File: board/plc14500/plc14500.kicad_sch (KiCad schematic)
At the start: 8 parts

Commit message: REV.D Schema updates
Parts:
- removed C? (x4): 100nF, Capacitor_THT:C_Rect_L7.2mm_W2.5mm_P5.00mm_FKS2_FKP2_MKS2_MKP2, symbol Device:C
- removed U? (x3): 74HC14, Package_DIP:DIP-14_W7.62mm_LongPads, symbol 74xx:74HC14
- removed U?: 4011, Package_DIP:DIP-14_W7.62mm_LongPads, symbol 4xxx:4011
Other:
- sheet Input/Output renamed Input-Output
- added sheet Programming Interface (programming_if.kicad_sch)
- sheet CPU ports: added A0, A1, A2, A3, A4, A5, A6, A7, D, D0, D1, D2, D3, D4, D5, D6, D7, PRG, RES, RR, W, WEN; removed none
- sheet Input-Output ports: added !RES, A0, A1, A2, A3, A4, A5, A6, A7, D, D0, D1, D2, D3, D4, D5, D6, D7, IN-INH, OUT-WD, OUT0, OUT1, OUT2, OUT3, OUT4, OUT5, OUT6, OUT7, PRG, RES, TMR0-TRG, WEN; removed none
- sheet SPRAM ports: added D, D4, D5, D6, D7, IN-INH, OUT-WD, RES, RR, W; removed none

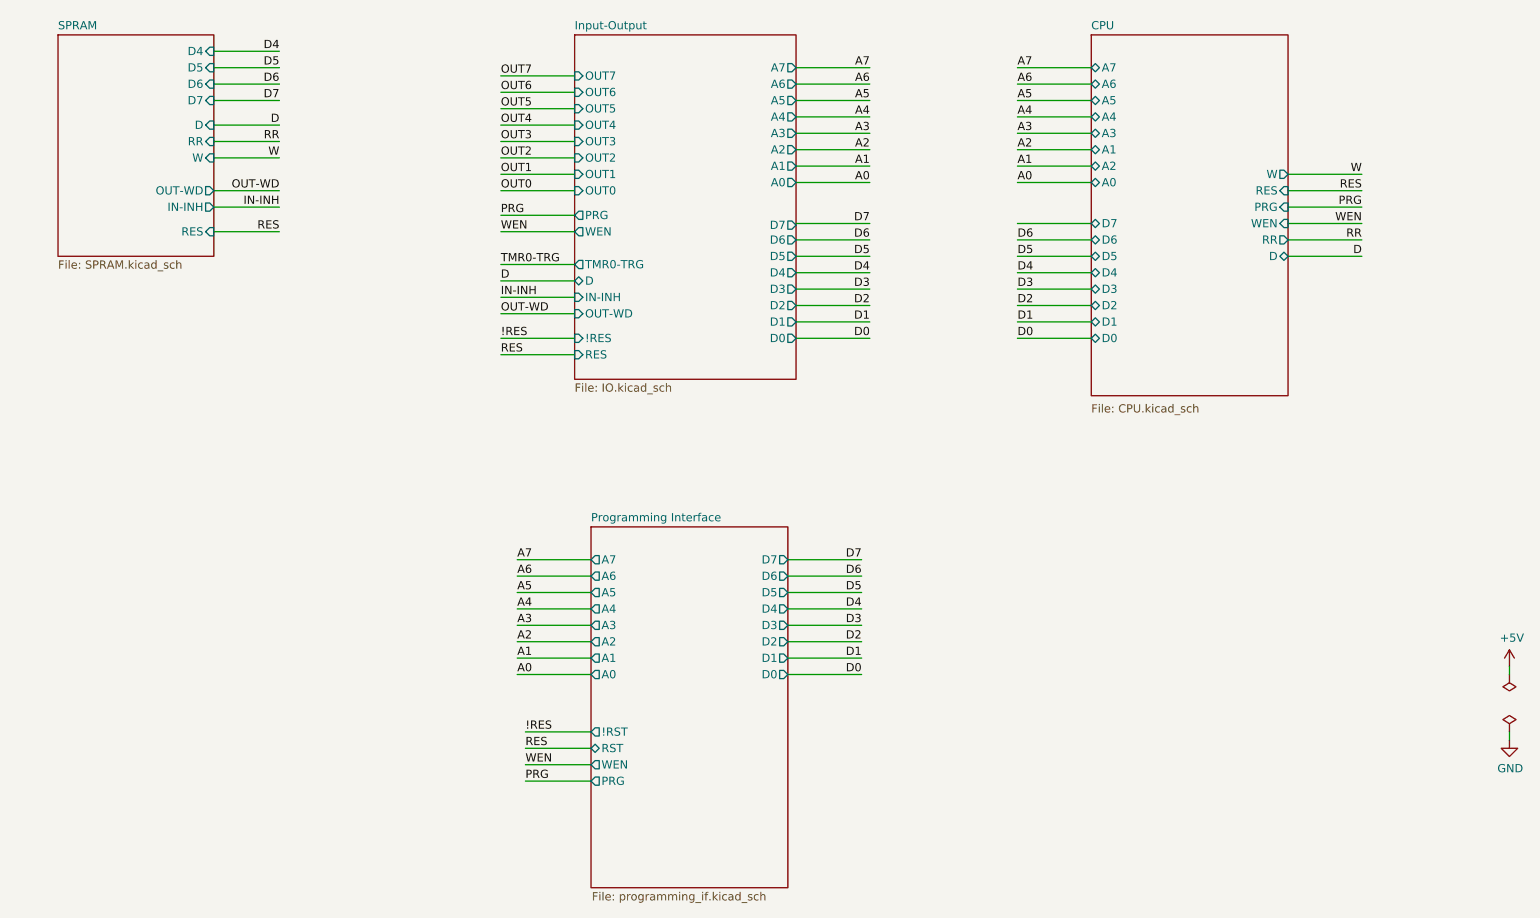
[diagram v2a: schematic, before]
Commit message: Address ERC errors
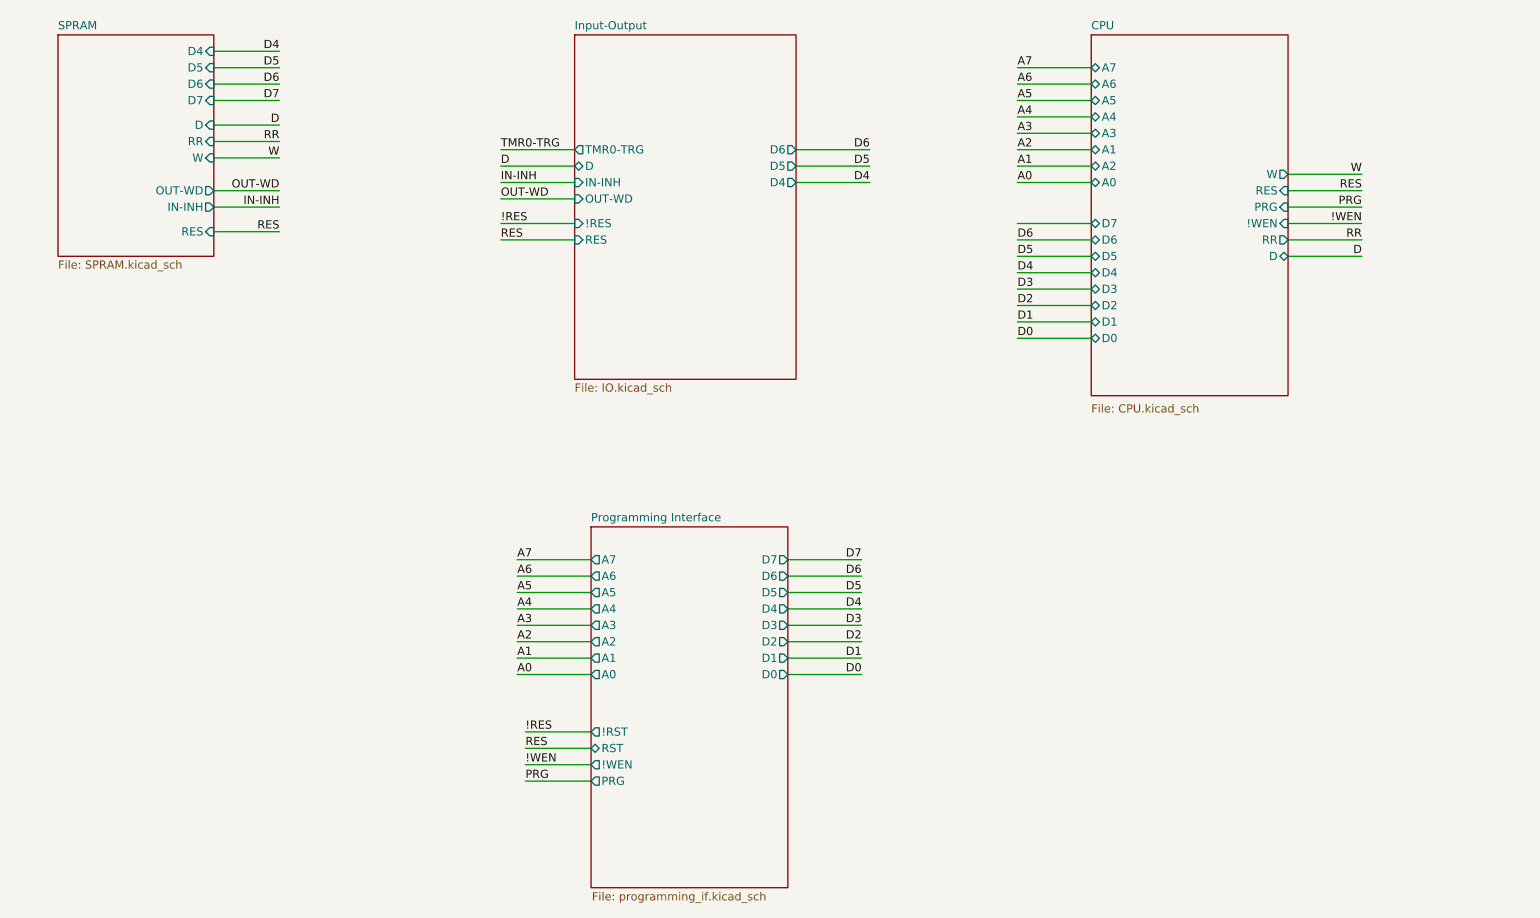
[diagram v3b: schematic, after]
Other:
- sheet CPU ports: added !WEN; removed WEN
- sheet Input-Output ports: added none; removed A0, A1, A2, A3, A4, A5, A6, A7, D0, D1, D2, D3, D7, OUT0, OUT1, OUT2, OUT3, OUT4, OUT5, OUT6, OUT7, PRG, WEN
- sheet Programming Interface ports: added !WEN; removed WEN

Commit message: Fix issues on REV.D0
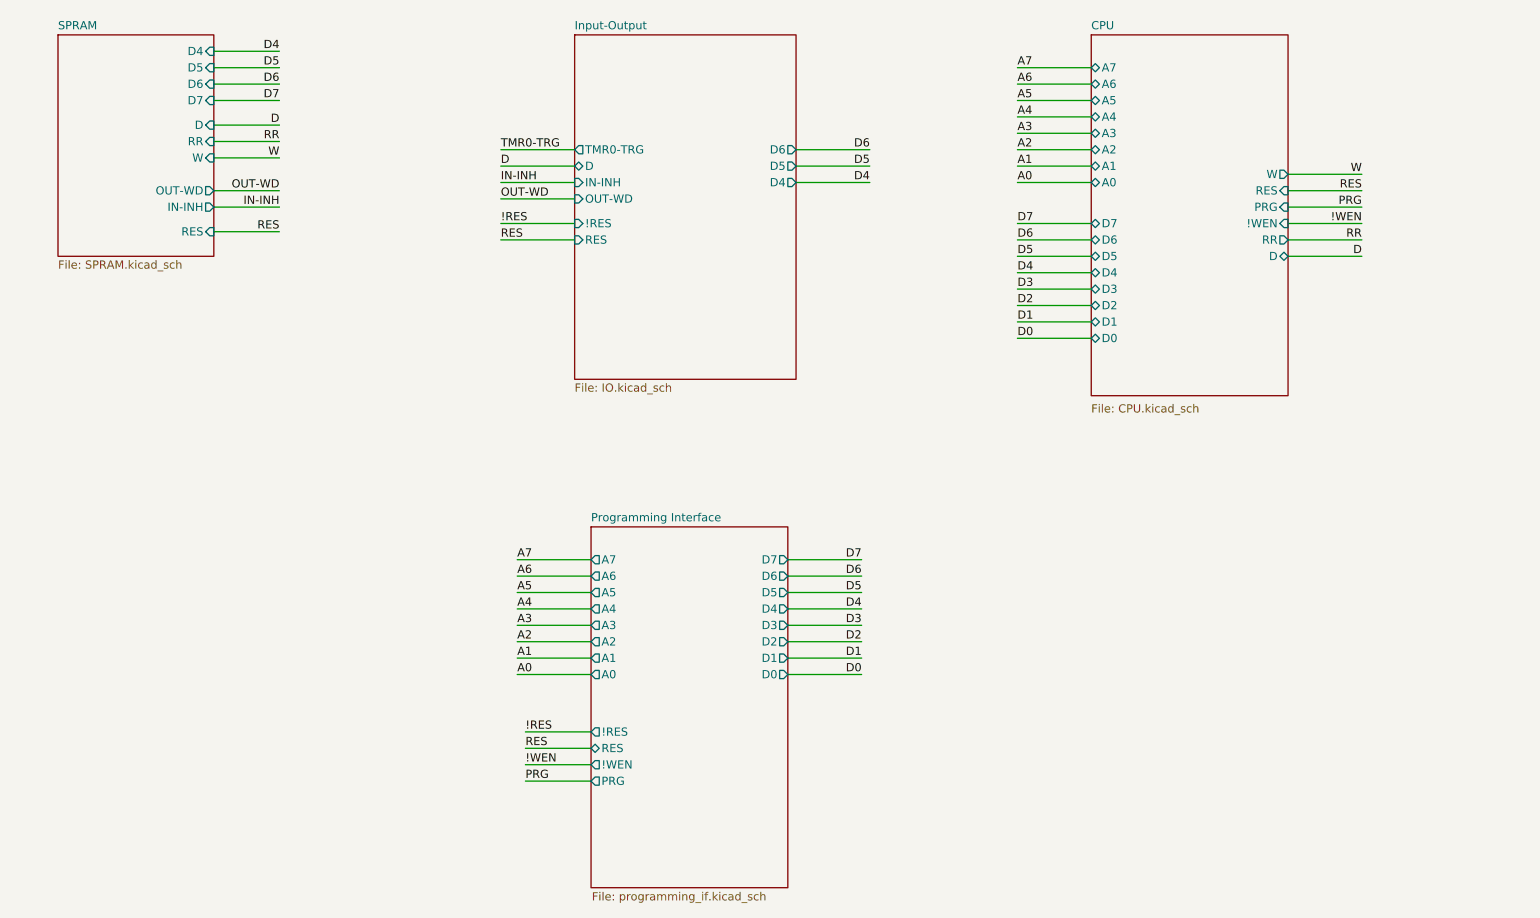
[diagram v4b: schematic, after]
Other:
- sheet Programming Interface ports: added !RES, RES; removed !RST, RST
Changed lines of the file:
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@@
+    (effects (font (size 1.27 1.27)) (justify left bottom))
+  )
+  (label "D7" (at 187.96 64.77 0) (fields_autoplaced)
     (effects (font (size 1.27 1.27)) (justify left bottom))
   )
@@
       (effects (font (size 1.27 1.27)) (justify left))
     )
-    (pin "A1" bidirectional (at 199.39 53.34 180)
-      (effects (font (size 1.27 1.27)) (justify left))
-    )
-    (pin "A2" bidirectional (at 199.39 55.88 180)
+    (pin "A1" bidirectional (at 199.39 55.88 180)
+      (effects (font (size 1.27 1.27)) (justify left))
+    )
+    (pin "A2" bidirectional (at 199.39 53.34 180)
       (effects (font (size 1.27 1.27)) (justify left))
     )
@@
       (effects (font (size 1.27 1.27)) (justify left))
     )
-    (pin "!RST" output (at 121.92 143.51 180)
-      (effects (font (size 1.27 1.27)) (justify left))
-    )
-    (pin "RST" bidirectional (at 121.92 146.05 180)
-      (effects (font (size 1.27 1.27)) (justify left))
-    )
+    (pin "RES" bidirectional (at 121.92 146.05 180)
+      (effects (font (size 1.27 1.27)) (justify left))
+    )
+    (pin "!RES" output (at 121.92 143.51 180)
+      (effects (font (size 1.27 1.27)) (justify left))
+    )
